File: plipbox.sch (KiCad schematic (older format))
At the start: 10 parts, among them P1 PWR, P2 PARALLEL_PORT, P3 RS232, U1 MAX3221, U2 ARDUINO_NANO_V3

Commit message: Use edge connector, use MAX232 & other minor tweaks
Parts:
- removed C3, C5: 330n, Capacitors_SMD:C_0603_HandSoldering, symbol C
- removed P2: PARALLEL_PORT, Keio:DB25M-RA-TH, symbol CONN_01X26
- removed U1: MAX3221, Housings_SSOP:TSSOP-16_4.4x5mm_Pitch0.65mm, symbol MAX3221
- removed U2: ARDUINO_NANO_V3, Keio:DIP-30_W15.24mm_LongPads, symbol ARDUINO_NANO_V3
- added C3, C4: 1u, Capacitor_SMD:C_0805_2012Metric_Pad1.18x1.45mm_HandSolder, symbol Device:CP1
- added P1: PARALLEL_PORT, Connector_Dsub:DSUB-25_Male_EdgeMount_P2.77mm, symbol Connector:DB25_Male
- added U1: ARDUINO_NANO_V3, plipbox:Arduino_Nano_Socket, symbol arduino:Arduino_Nano_Socket
- added U2: MAX232, Package_SO:SOIC-16_3.9x9.9mm_P1.27mm, symbol Interface_UART:MAX232
- added V0: OSHW_LOGO, Symbol:OSHW-Logo2_9.8x8mm_Copper, symbol void:Void
- C1: value 47n -> 1u; footprint Capacitors_SMD:C_0603_HandSoldering -> Capacitor_SMD:C_0805_2012Metric_Pad1.18x1.45mm_HandSolder; symbol C -> plipbox-rescue:C
- C2: renamed from C4; value 330n -> 1u; footprint Capacitors_SMD:C_0603_HandSoldering -> Capacitor_SMD:C_0805_2012Metric_Pad1.18x1.45mm_HandSolder; symbol C -> plipbox-rescue:C
- C5: renamed from C2; value 100n -> 1u; footprint Capacitors_SMD:C_0603_HandSoldering -> Capacitor_SMD:C_0805_2012Metric_Pad1.18x1.45mm_HandSolder; symbol C -> plipbox-rescue:C
- P2: renamed from P1; footprint Pin_Headers:Pin_Header_Straight_1x03_Pitch2.54mm -> plipbox:Pin_Header_Straight_1x03-ModSilkS; symbol CONN_01X03 -> plipbox-rescue:CONN_01X03
- P3: footprint Pin_Headers:Pin_Header_Straight_1x03_Pitch2.54mm -> plipbox:Pin_Header_Straight_1x03-ModSilkS; symbol CONN_01X03 -> plipbox-rescue:CONN_01X03
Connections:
- wire segments 79 -> 88
- no-connect marks 18 -> 21
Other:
- moved on the sheet: C1, C2, C5, P2

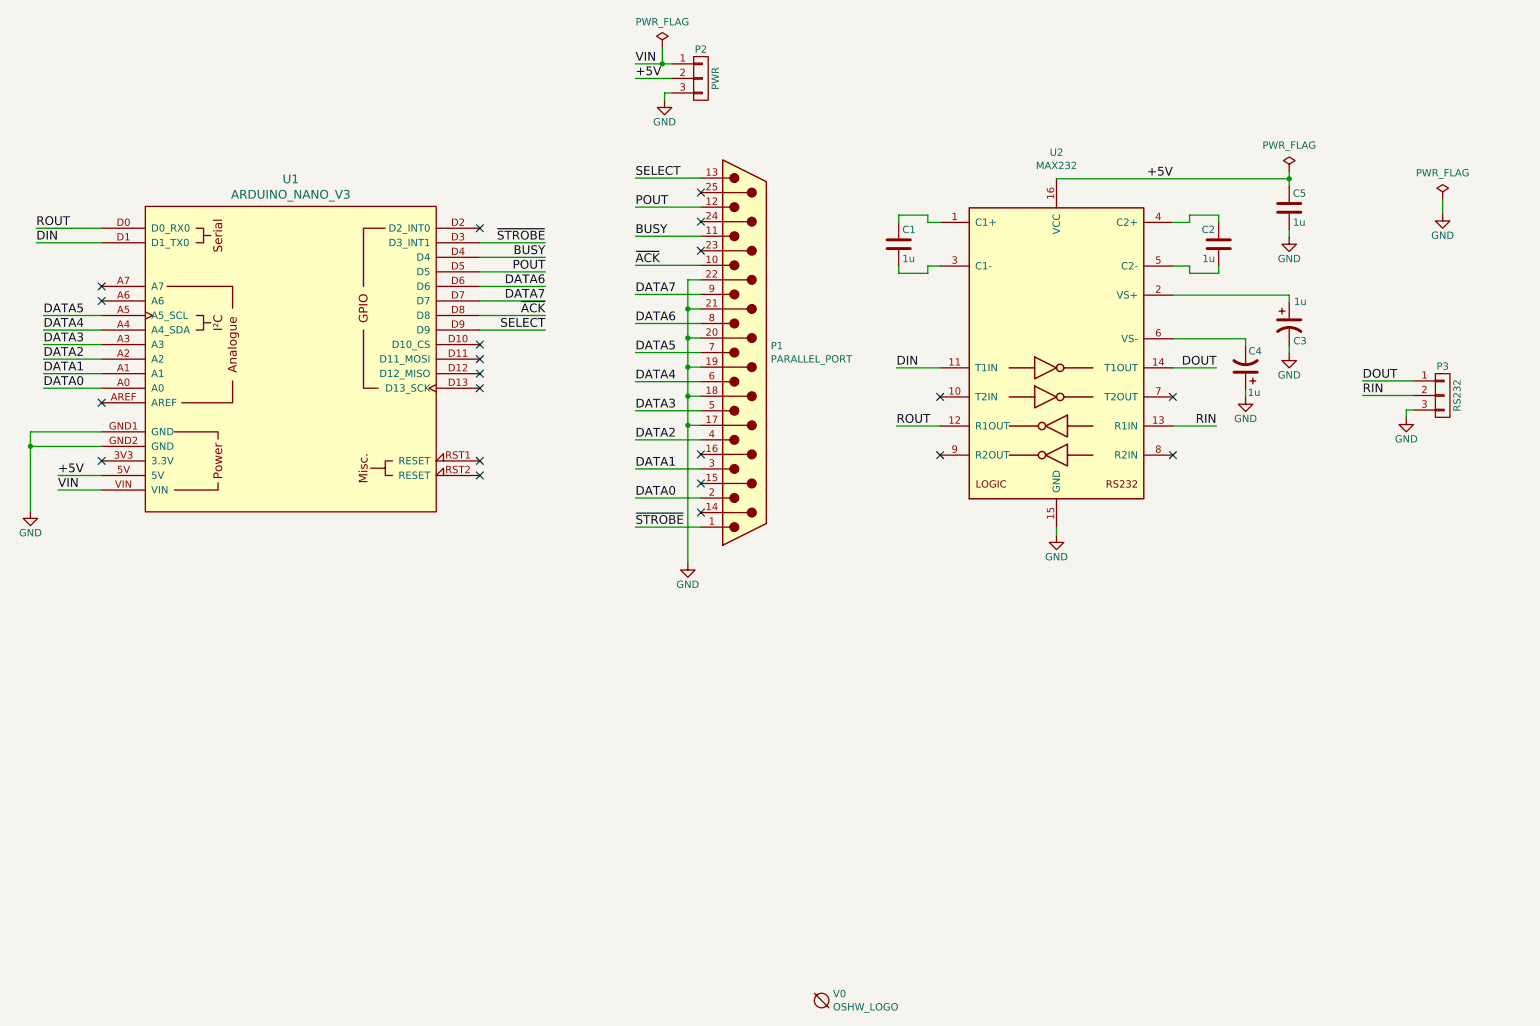
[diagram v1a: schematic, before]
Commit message: Add diode and fix C3 C3 was WRONG in Rev.1S, it needs to be between pin 2 of U1 and VCC, not GND. The diode should only be mounted if the Amiga is modded so that power on the +5V line is not limited.
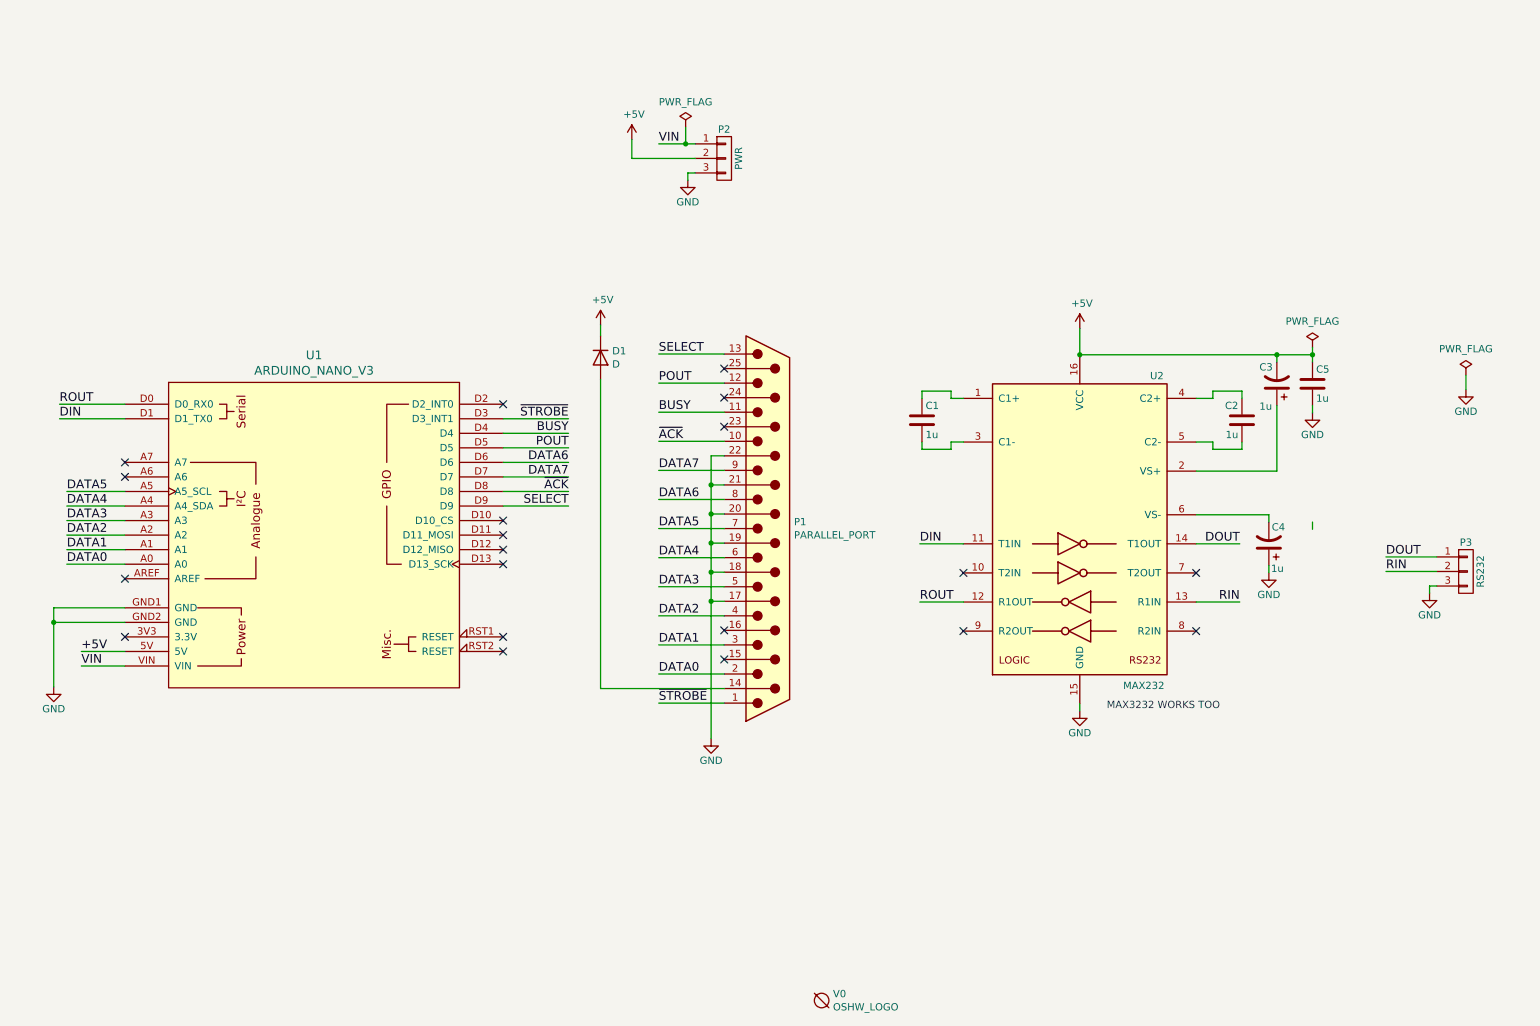
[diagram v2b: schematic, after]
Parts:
- added D1: D, Diode_SMD:D_SMA, symbol Device:D
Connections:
- net +5V: now also C3.2, D1.1 (K)
- net GND: no longer C3.2
- net at P1.14 (P14): now also D1.2 (A)
- no-connect marks 21 -> 20
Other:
- note added: "MAX3232 WORKS TOO"
- moved on the sheet: C1, C2, C3, C4, C5, P1, P2, P3, U1, U2

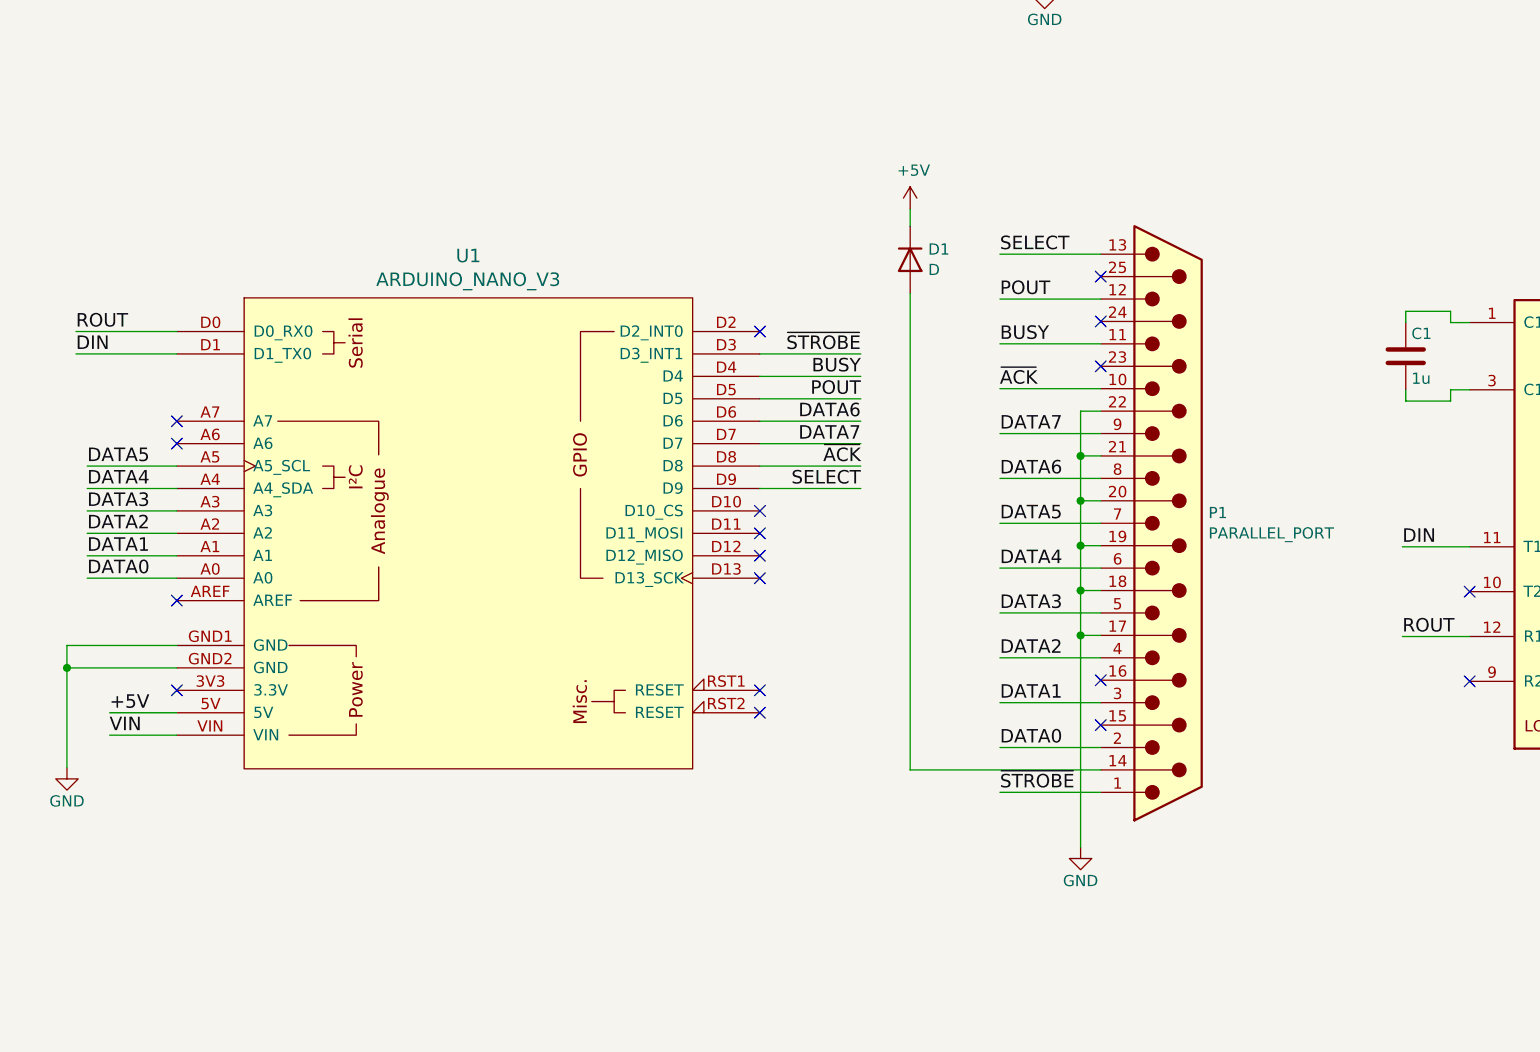
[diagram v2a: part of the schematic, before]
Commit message: Add reset jumper and ready for V2S
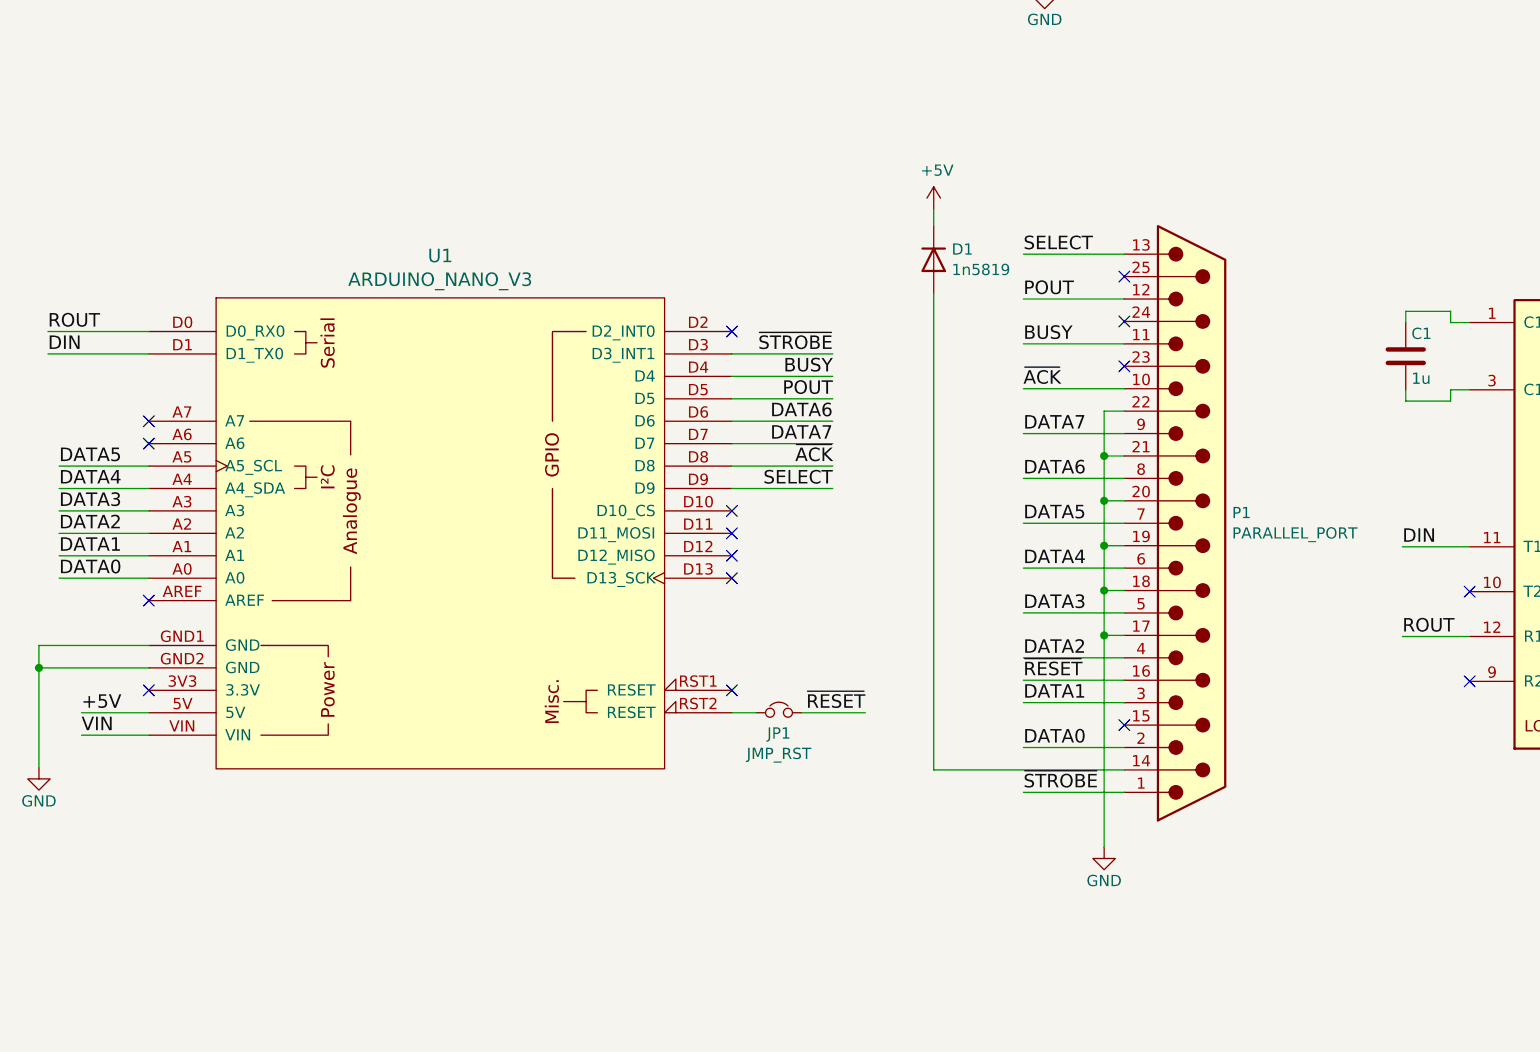
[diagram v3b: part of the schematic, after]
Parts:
- added JP1: JMP_RST, Jumper:SolderJumper-2_P1.3mm_Open_RoundedPad1.0x1.5mm, symbol Device:Jumper_NC_Small
- D1: value D -> 1n5819
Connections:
- net ~RESET: now reaches P1.16 (P16)
- net ~RESET: now also JP1.2
- net at U1.RST2 (RESET): now also JP1.1
- no-connect marks 20 -> 18
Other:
- moved on the sheet: D1, P1, U1
